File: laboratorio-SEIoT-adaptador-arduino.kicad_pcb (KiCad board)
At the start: 2 copper layers, 92.1 x 100.5 mm, 7 parts, among them J1 Conn_01x08, J2 Conn_01x10, J3 Conn_01x06, J4 Conn_01x08, U3 FRANZININHO_WIFI_PINOUT

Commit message: adição de licensa
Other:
- board text added: "Licensed under CERN-OHL-S v2"
- board text added: "SOURCE: github.com/Franzininho/laboratorio-SEIoT-adaptador-arduino"
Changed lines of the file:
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@@
   (gr_line (start 182.8375 109.8875) (end 168.9625 109.9125)
     (stroke (width 0.2) (type solid)) (layer "Edge.Cuts"))
+  (gr_text "Licensed under CERN-OHL-S v2" (at 167.5892 151.1554) (layer "B.SilkS")
+    (effects (font (size 1 1) (thickness 0.15)) (justify left bottom mirror))
+  )
+  (gr_text "SOURCE: github.com/Franzininho/laboratorio-SEIoT-adaptador-arduino" (at 181.2798 55.0672) (layer "B.SilkS")
+    (effects (font (size 1 1) (thickness 0.15)) (justify left bottom mirror))
+  )
   (gr_text "AC" (at 150.65 98) (layer "F.SilkS")
     (effects (font (size 1.2 1.2) (thickness 0.25)))

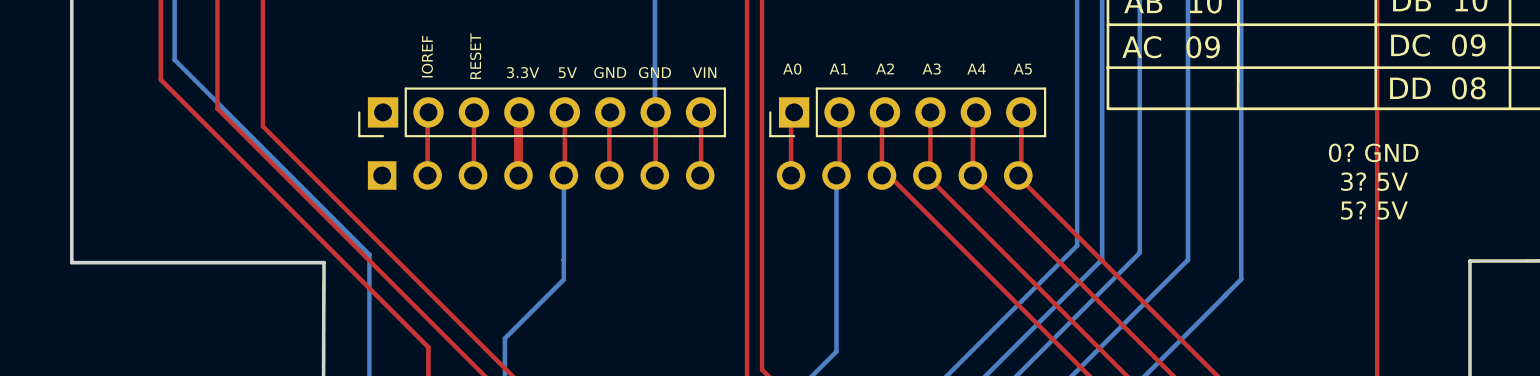
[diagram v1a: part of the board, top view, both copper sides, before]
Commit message: adicionada certificação OSHWA
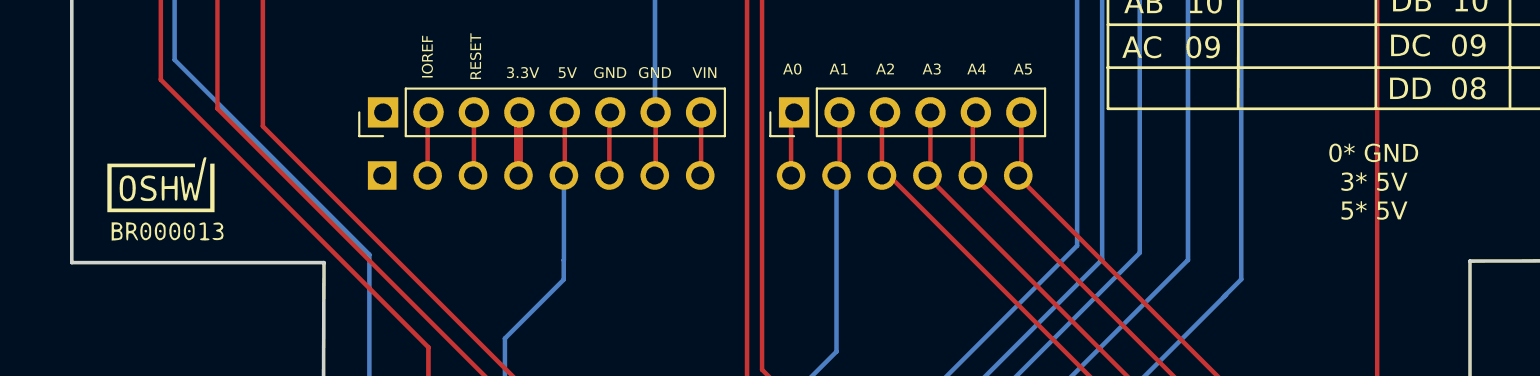
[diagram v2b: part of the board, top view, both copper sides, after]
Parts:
- added G1: LOGO, LOGO, F.Cu at (95.8, 106.5)
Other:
- board text added: "0* GND 3* 5V 5* 5V"
- board text removed: "0? GND 3? 5V 5? 5V"
